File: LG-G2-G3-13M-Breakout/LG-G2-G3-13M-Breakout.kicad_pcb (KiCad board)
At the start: 2 copper layers, 45.7 x 68.6 mm, 8 parts, among them P1 LG-G2-G3-Rear-Camera, P2 CONN_02X08, P3 CONN_01X03, P4 CONN_01X03, P5 CONN_01X02, P6 CONN_01X03, P7 CONN_01X02, P8 CONN_01X04

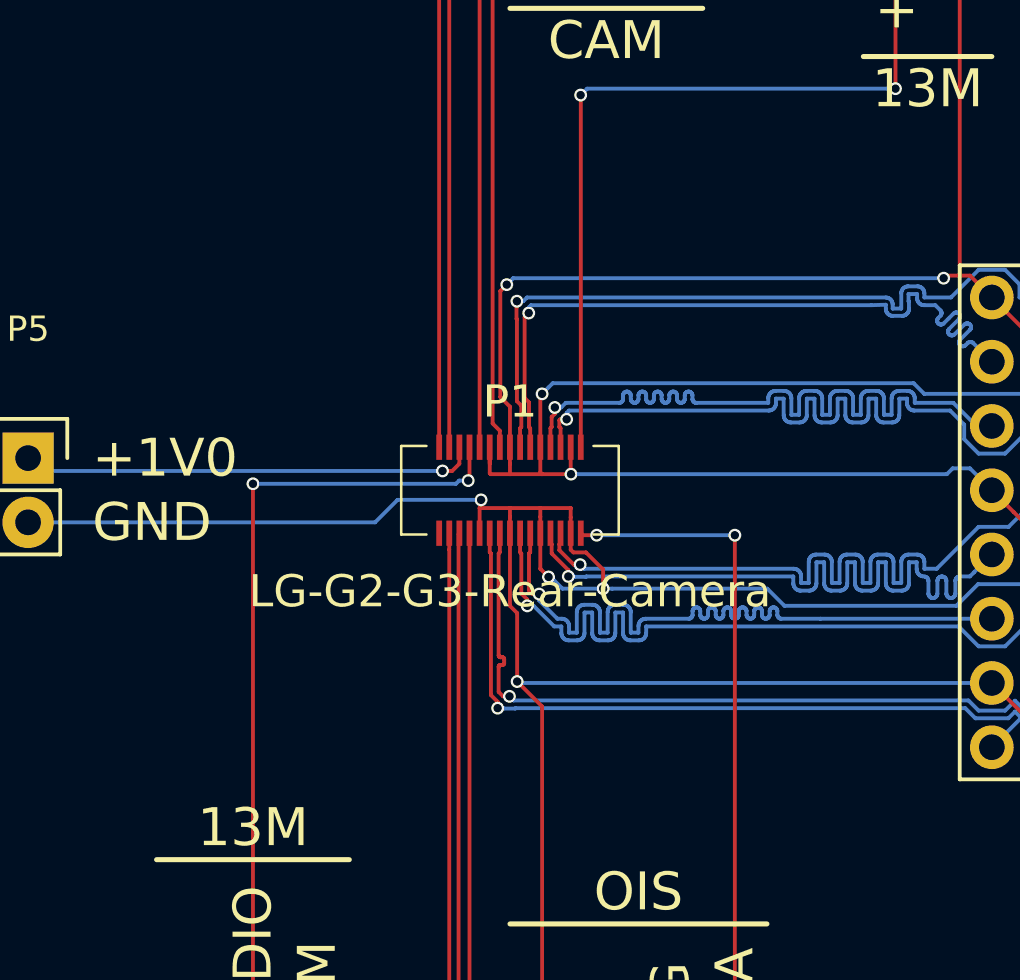
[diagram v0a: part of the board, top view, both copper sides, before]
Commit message: Switched to the new component library
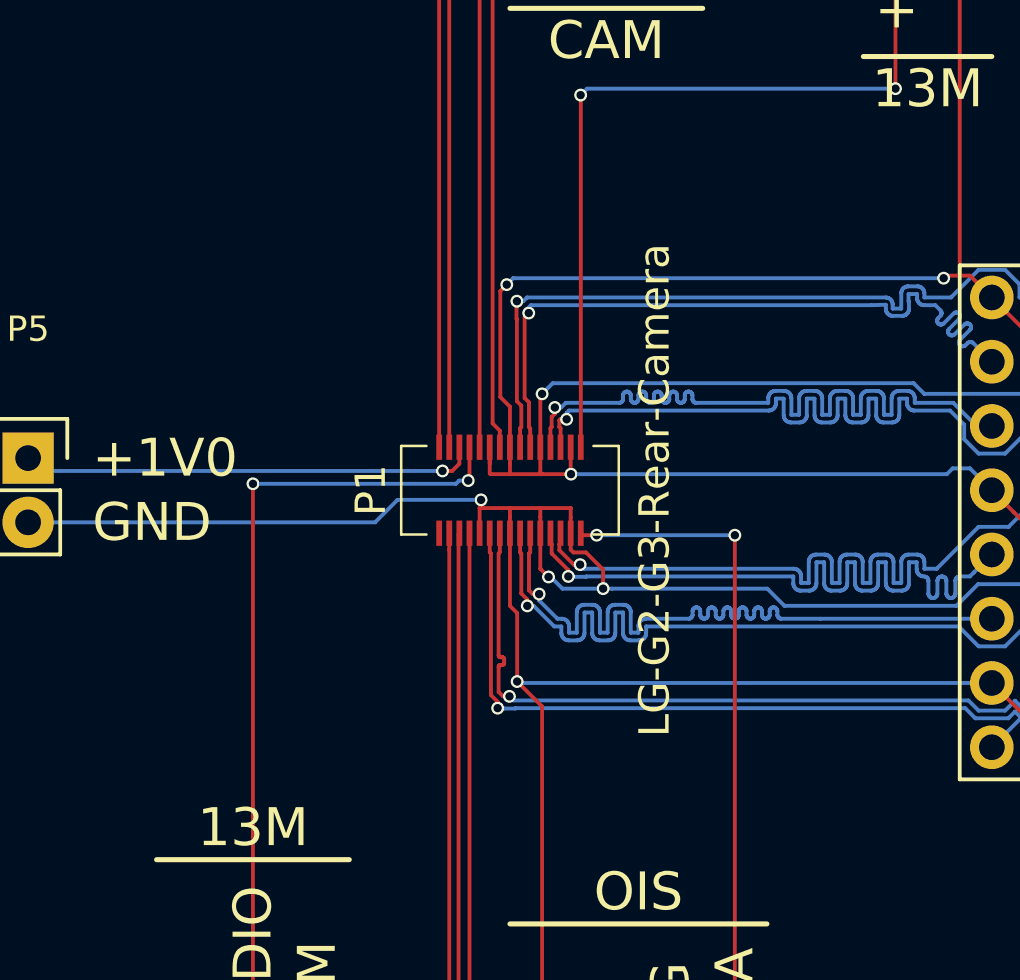
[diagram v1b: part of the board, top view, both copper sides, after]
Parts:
- P1: footprint HDMI-to-MIPI:GB042-30S -> connectors:GB042-30S
